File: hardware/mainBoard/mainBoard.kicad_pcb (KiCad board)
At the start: 2 copper layers, 99.9 x 49.9 mm, 22 parts, among them J1 DisplayConnector, J2 LeftKeyConnector, J3 RightKeyConnector, J4 EncoderConnector

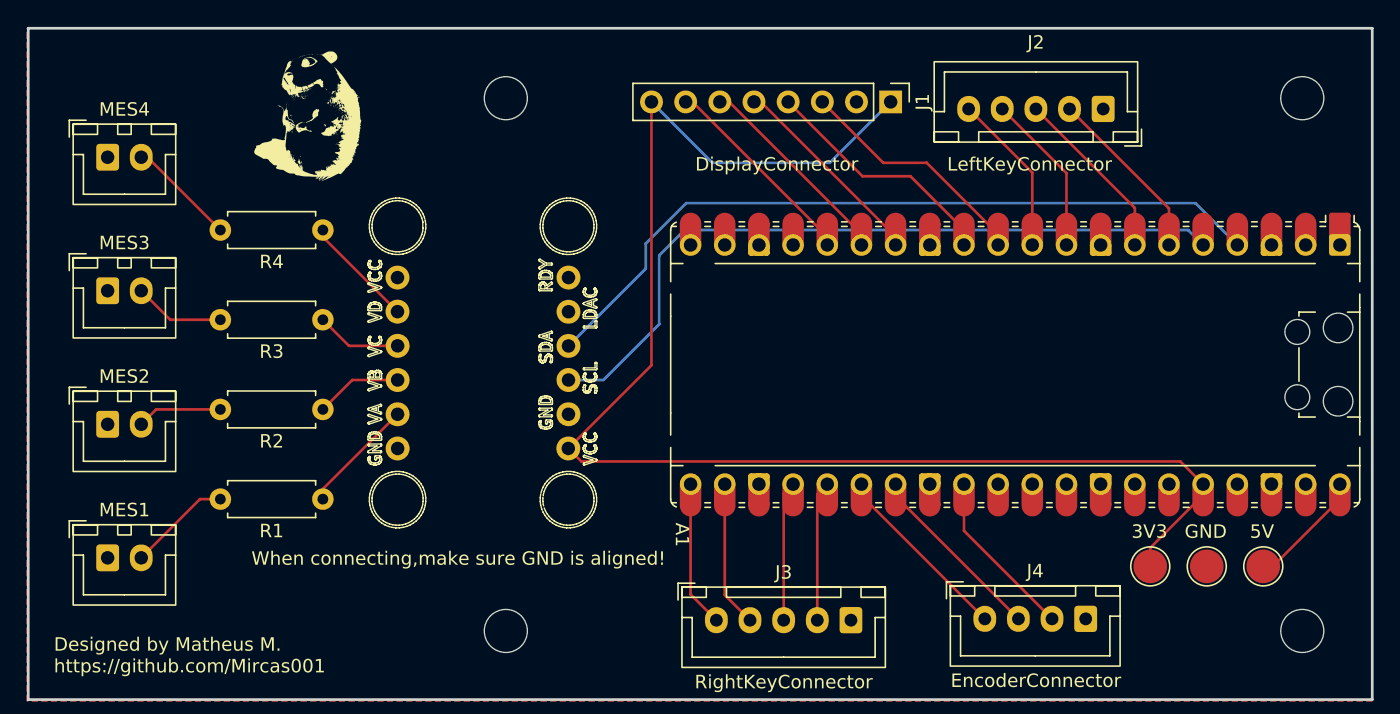
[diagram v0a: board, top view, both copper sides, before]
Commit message: Switched from prebuilt module to chip
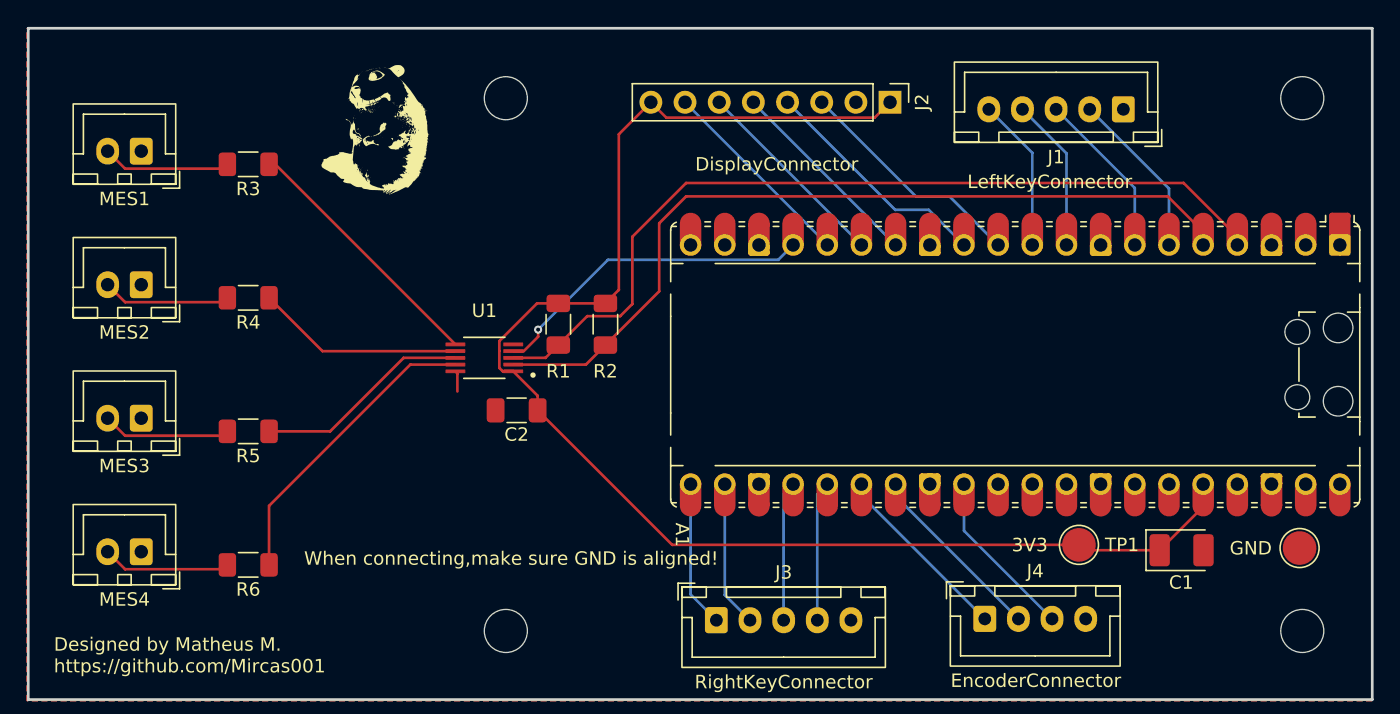
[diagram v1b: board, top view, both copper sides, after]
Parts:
- removed TP3: TestPoint, TestPoint:TestPoint_Pad_D2.5mm
- added C1: 10µF, Capacitor_Tantalum_SMD:CP_EIA-3528-15_AVX-H_HandSolder, F.Cu at (193.8, 108.8)
- added C2: 0.1μF, Capacitor_SMD:C_1206_3216Metric_Pad1.33x1.80mm_HandSolder, F.Cu at (144.4, 98.4)
- added R5: 680, Resistor_SMD:R_1206_3216Metric_Pad1.30x1.75mm_HandSolder, F.Cu at (124.5, 100.0)
- added R6: 680, Resistor_SMD:R_1206_3216Metric_Pad1.30x1.75mm_HandSolder, F.Cu at (124.5, 109.9)
- J1: value DisplayConnector -> LeftKeyConnector; footprint Connector_PinHeader_2.54mm:PinHeader_1x08_P2.54mm_Vertical -> Connector_JST:JST_XH_B5B-XH-A_1x05_P2.50mm_Vertical
- J2: value LeftKeyConnector -> DisplayConnector; footprint Connector_JST:JST_XH_B5B-XH-A_1x05_P2.50mm_Vertical -> Connector_PinHeader_2.54mm:PinHeader_1x08_P2.54mm_Vertical
- R1, R2: value 680 -> 10K; footprint Resistor_THT:R_Axial_DIN0207_L6.3mm_D2.5mm_P7.62mm_Horizontal -> Resistor_SMD:R_1206_3216Metric_Pad1.30x1.75mm_HandSolder
- R3, R4: footprint Resistor_THT:R_Axial_DIN0207_L6.3mm_D2.5mm_P7.62mm_Horizontal -> Resistor_SMD:R_1206_3216Metric_Pad1.30x1.75mm_HandSolder
- U1: value ~ -> MCP4728-E_UN; footprint Adafruit_MCP4728:Adafruit_MCP4728 -> Snapeda:SOP50P490X110-10N
- moved MES1 30.3 mm to (116.5, 79.1), turned to 180 degrees
- moved MES4 29.4 mm to (116.5, 108.9), turned to 180 degrees
- moved R2 21.9 mm to (151.0, 92.0), turned to -90 degrees
- moved R1 21.8 mm to (147.5, 92.0), turned to -90 degrees
- moved J1 17.3 mm to (189.5, 76.0), turned to 180 degrees
- moved J2 15.8 mm to (172.2, 75.5), turned to -90 degrees
- moved U1 15.8 mm to (142.0, 94.5), turned to 180 degrees
- moved TP1 13.8 mm to (186.2, 108.4), turned to 0 degrees
- moved R3 12.8 mm to (124.5, 80.1)
- moved MES2 10.7 mm to (116.5, 89.1), turned to 180 degrees
- moved MES3 9.80 mm to (116.5, 99.0), turned to 180 degrees
- moved R4 7.50 mm to (124.5, 90.0)
- moved TP2 7.03 mm to (202.6, 108.6)
- moved G*** 5.10 mm to (134.0, 78.0)
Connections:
- A1 pad 17: unconnected-(A1-GPIO13-Pad17) -> /LDAC
- J1 pad 1: +3V3 -> GND
- J1 pad 2: GND -> Net-(A1-GPIO4)
- J1 pad 3: Net-(A1-GPIO8) -> Net-(A1-GPIO5)
- J1 pad 4: Net-(A1-GPIO9) -> Net-(A1-GPIO6)
- J1 pad 5: Net-(A1-GPIO10) -> Net-(A1-GPIO7)
- J2 pad 1: GND -> +3V3
- J2 pad 2: Net-(A1-GPIO4) -> GND
- J2 pad 3: Net-(A1-GPIO5) -> Net-(A1-GPIO8)
- J2 pad 4: Net-(A1-GPIO6) -> Net-(A1-GPIO9)
- J2 pad 5: Net-(A1-GPIO7) -> Net-(A1-GPIO10)
- R1 pad 1: Net-(U1-VA) -> +3V3
- R1 pad 2: Net-(MES1-+) -> SDA
- R2 pad 1: Net-(U1-VB) -> +3V3
- R2 pad 2: Net-(MES2-+) -> SCL
- R3 pad 1: Net-(U1-VC) -> Net-(U1-VOUTA)
- R3 pad 2: Net-(MES3-+) -> Net-(MES1-+)
- R4 pad 1: Net-(U1-VD) -> Net-(U1-VOUTB)
- R4 pad 2: Net-(MES4-+) -> Net-(MES2-+)
- TP1 pad 1: +5V -> +3V3
- U1 pad 1: GND -> +3V3
- U1 pad 10: SDA -> GND
- U1 pad 2: Net-(U1-VA) -> SCL
- U1 pad 3: Net-(U1-VB) -> SDA
- U1 pad 4: Net-(U1-VC) -> /LDAC
- U1 pad 5: Net-(U1-VD) -> unconnected-(U1-RDY/*BSY-Pad5)
- U1 pad 6: unconnected-(U1-VCC-Pad6) -> Net-(U1-VOUTA)
- U1 pad 7: +3V3 -> Net-(U1-VOUTB)
- U1 pad 8: GND -> Net-(U1-VOUTC)
- U1 pad 9: SCL -> Net-(U1-VOUTD)
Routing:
- net /LDAC: track 0.00 -> 24.4 mm, vias 0 -> 1
- net Net-(U1-VOUTD): track 0.00 -> 22.6 mm
- net Net-(U1-VOUTA): track 0.00 -> 19.4 mm
- net Net-(U1-VOUTC): track 0.00 -> 16.1 mm
- net Net-(U1-VOUTB): track 0.00 -> 15.5 mm
- net +5V: track 9.61 -> 0.73 mm
- net Net-(U1-VA): track 8.61 -> 0.00 mm
- net Net-(U1-VD): track 8.36 -> 0.00 mm
- net SDA: track 56.5 -> 64.4 mm
- net Net-(U1-VB): track 6.46 -> 0.00 mm
- net Net-(U1-VC): track 6.36 -> 0.00 mm
- net SCL: track 55.2 -> 61.5 mm
- net Net-(MES2-+): track 6.34 -> 9.57 mm
- net Net-(MES3-+): track 6.77 -> 9.57 mm
- net +3V3: track 105.5 -> 107.7 mm
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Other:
- board text removed: "5V"

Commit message: update README.md to have kicanvas and 3d model image, also fix main board PCB
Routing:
- net +3V3: track 107.7 -> 123.9 mm, vias 0 -> 1
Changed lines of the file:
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@@
 	)
 	(footprint "Snapeda:SOP50P490X110-10N"
-		(locked yes)
 		(layer "F.Cu")
 		(at 142 94.5 180)
@@
 			)
 		)
-		(pad "1" thru_hole rect
+		(pad "1" thru_hole oval
 			(at 0 0 270)
 			(size 1.7 1.7)
@@
 			(pintype "passive")
 		)
-		(pad "2" thru_hole circle
-			(at 0 2.54 270)
+		(pad "2" thru_hole roundrect
+			(at 0 2.54)
 			(size 1.7 1.7)
 			(drill 1)
 			(layers "*.Cu" "*.Mask")
 			(remove_unused_layers no)
+			(roundrect_rratio 0.1470588235)
 			(net "GND")
 			(pinfunction "Pin_2_2")
@@
 	)
 	(segment
-		(start 154.38 75.5)
-		(end 155.53 76.65)
+		(start 159.48 80.6)
+		(end 154.38 75.5)
 		(width 0.2)
 		(layer "F.Cu")
@@
 	)
 	(segment
-		(start 155.53 76.65)
-		(end 171.01 76.65)
-		(width 0.2)
-		(layer "F.Cu")
-		(net "+3V3")
-	)
-	(segment
 		(start 143.115 94)
 		(end 143.115 95.244732)
@@
 	)
 	(segment
+		(start 178.6 80.6)
+		(end 159.48 80.6)
+		(width 0.2)
+		(layer "F.Cu")
+		(net "+3V3")
+	)
+	(segment
 		(start 152 77.88)
 		(end 154.38 75.5)
@@
 	)
 	(segment
-		(start 171.01 76.65)
-		(end 172.16 75.5)
-		(width 0.2)
-		(layer "F.Cu")
-		(net "+3V3")
-	)
-	(segment
 		(start 192.2 108.8)
 		(end 195.4325 105.5675)
@@
 		(net "+3V3")
 	)
+	(via
+		(at 178.6 80.6)
+		(size 0.6)
+		(drill 0.3)
+		(layers "F.Cu" "B.Cu")
+		(net "+3V3")
+	)
+	(segment
+		(start 175.2 77.2)
+		(end 173.86 77.2)
+		(width 0.2)
+		(layer "B.Cu")
+		(net "+3V3")
+	)
+	(segment
+		(start 173.86 77.2)
+		(end 172.16 75.5)
+		(width 0.2)
+		(layer "B.Cu")
+		(net "+3V3")
+	)
+	(segment
+		(start 178.6 80.6)
+		(end 175.2 77.2)
+		(width 0.2)
+		(layer "B.Cu")
+		(net "+3V3")
+	)

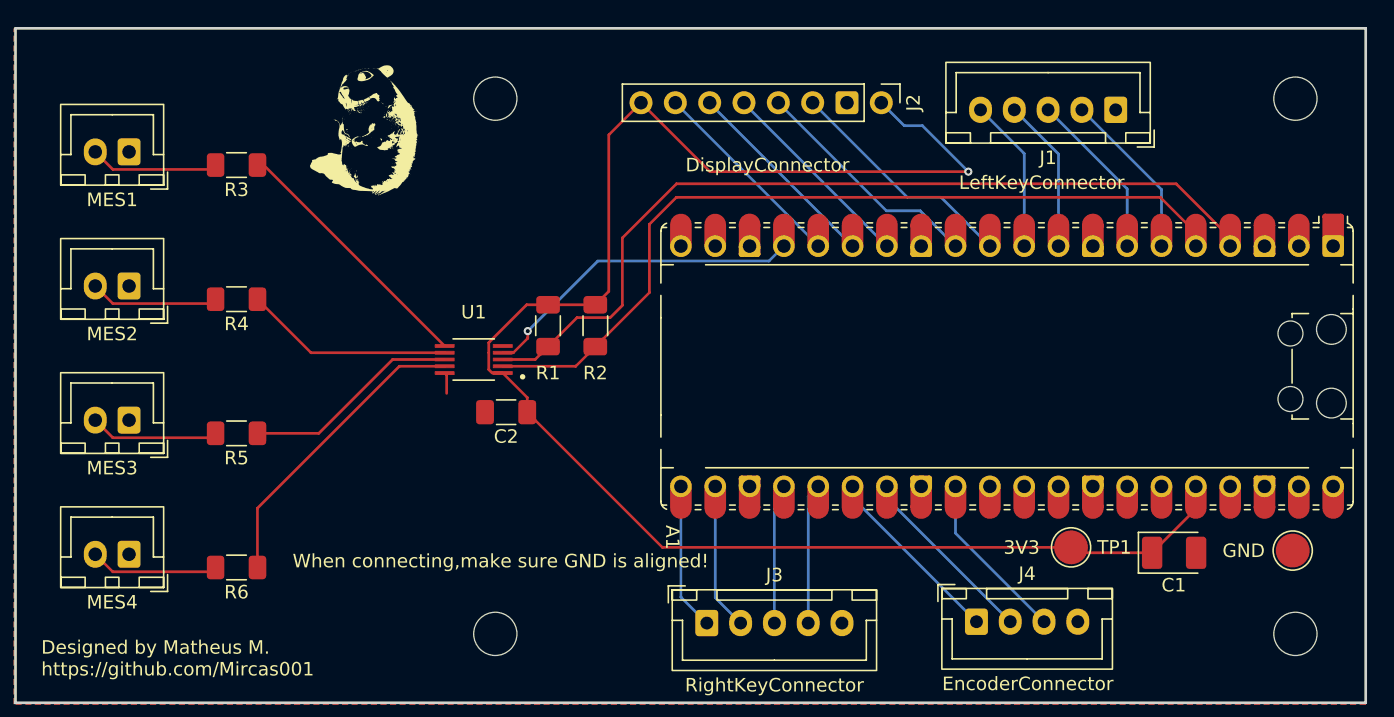
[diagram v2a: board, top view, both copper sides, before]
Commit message: Label the connectors in the silkscreen
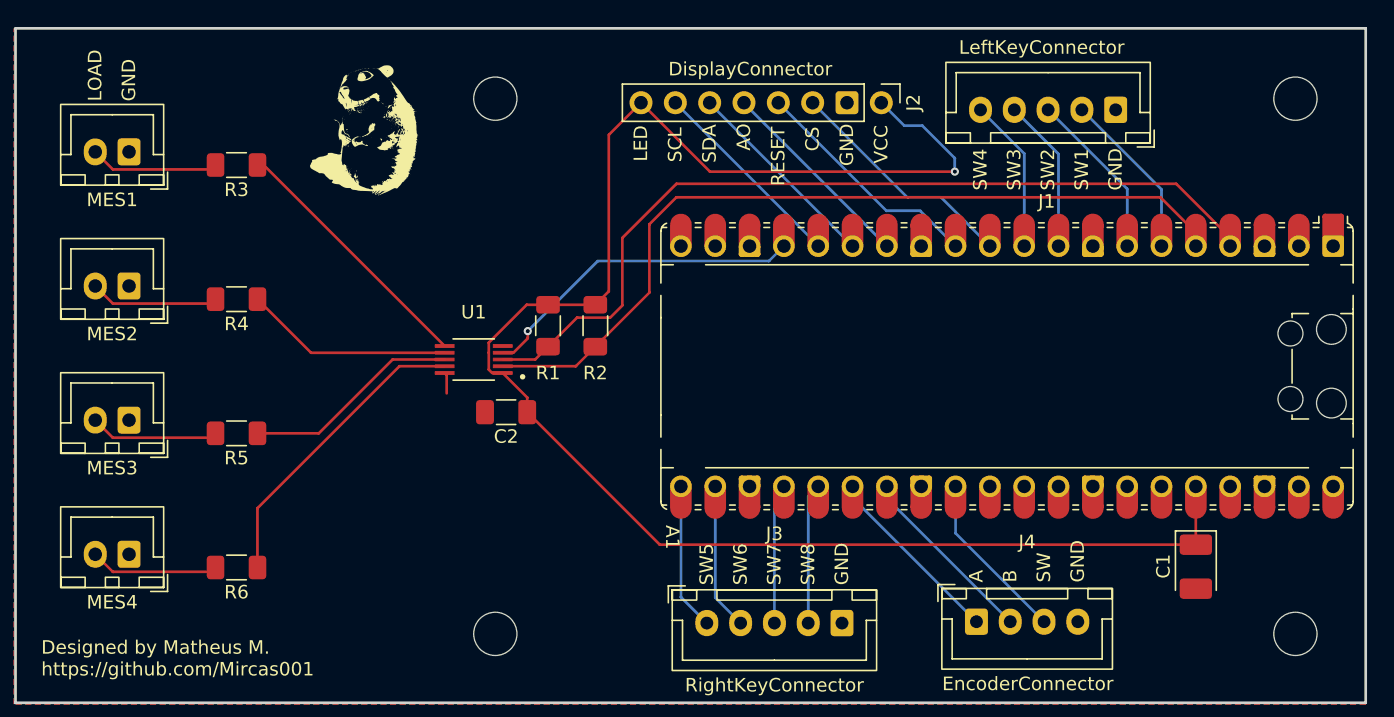
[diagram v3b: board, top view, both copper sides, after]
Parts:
- removed TP1, TP2: TestPoint, TestPoint:TestPoint_Pad_D2.5mm
- moved C1 1.91 mm to (195.4, 109.8), turned to -90 degrees
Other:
- board text added: "A"
- board text added: "AO"
- board text added: "B"
- board text added: "CS"
- board text added: "LED"
- board text added: "LOAD"
- board text added: "RESET"
- board text added: "SCL"
- board text added: "SDA"
- board text added: "SW"
- board text added: "SW1"
- board text added: "SW2"
- board text added: "SW3"
- board text added: "SW4"
- board text added: "SW5"
- board text added: "SW6"
- board text added: "SW7"
- board text added: "SW8"
- board text added: "VCC"
- board text removed: "3V3"
- board text removed: "When connecting,make sure GND is aligned!"

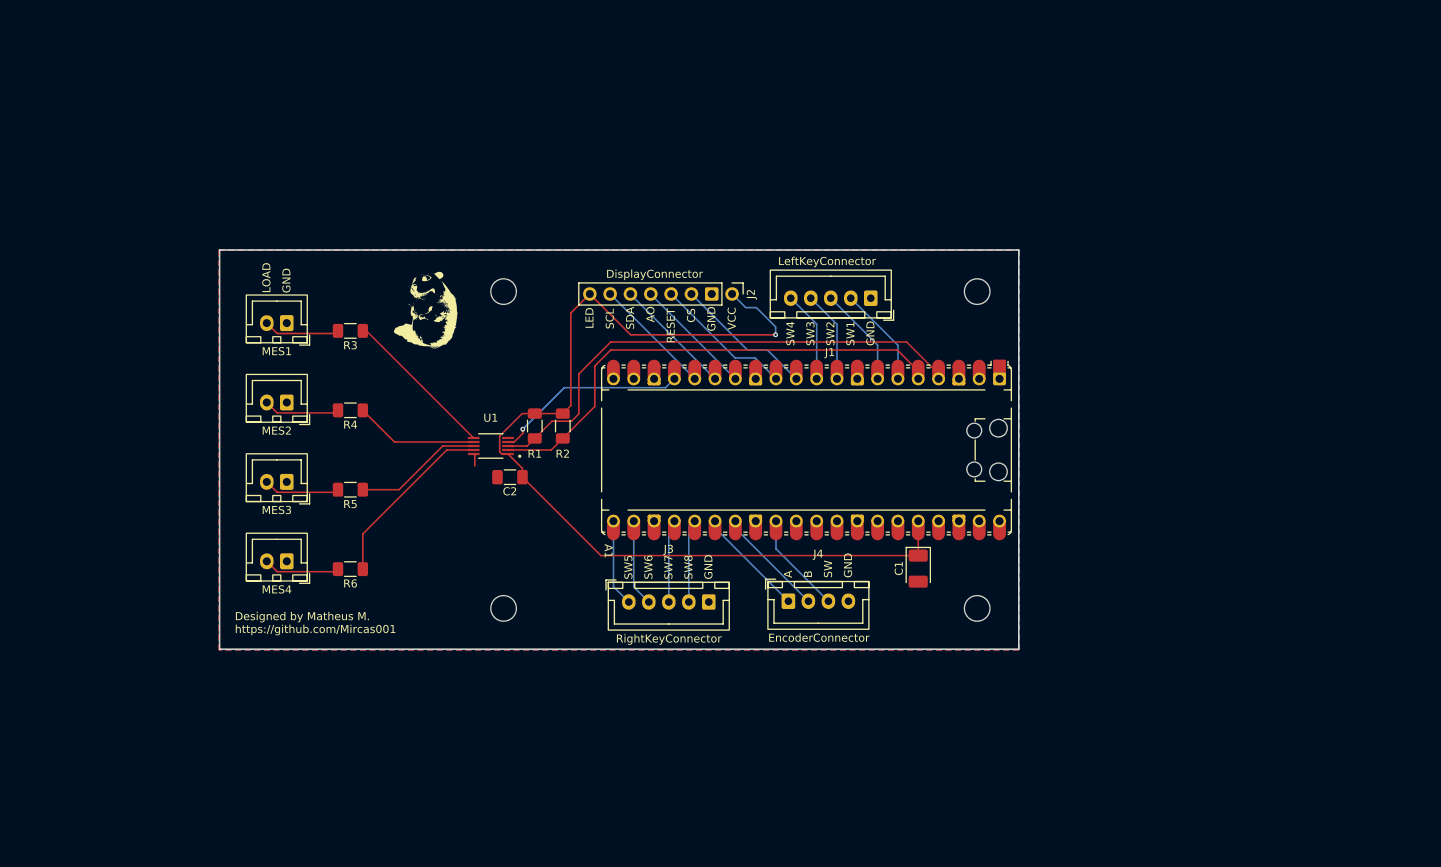
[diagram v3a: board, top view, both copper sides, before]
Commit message: update PCB routing and add debug probe
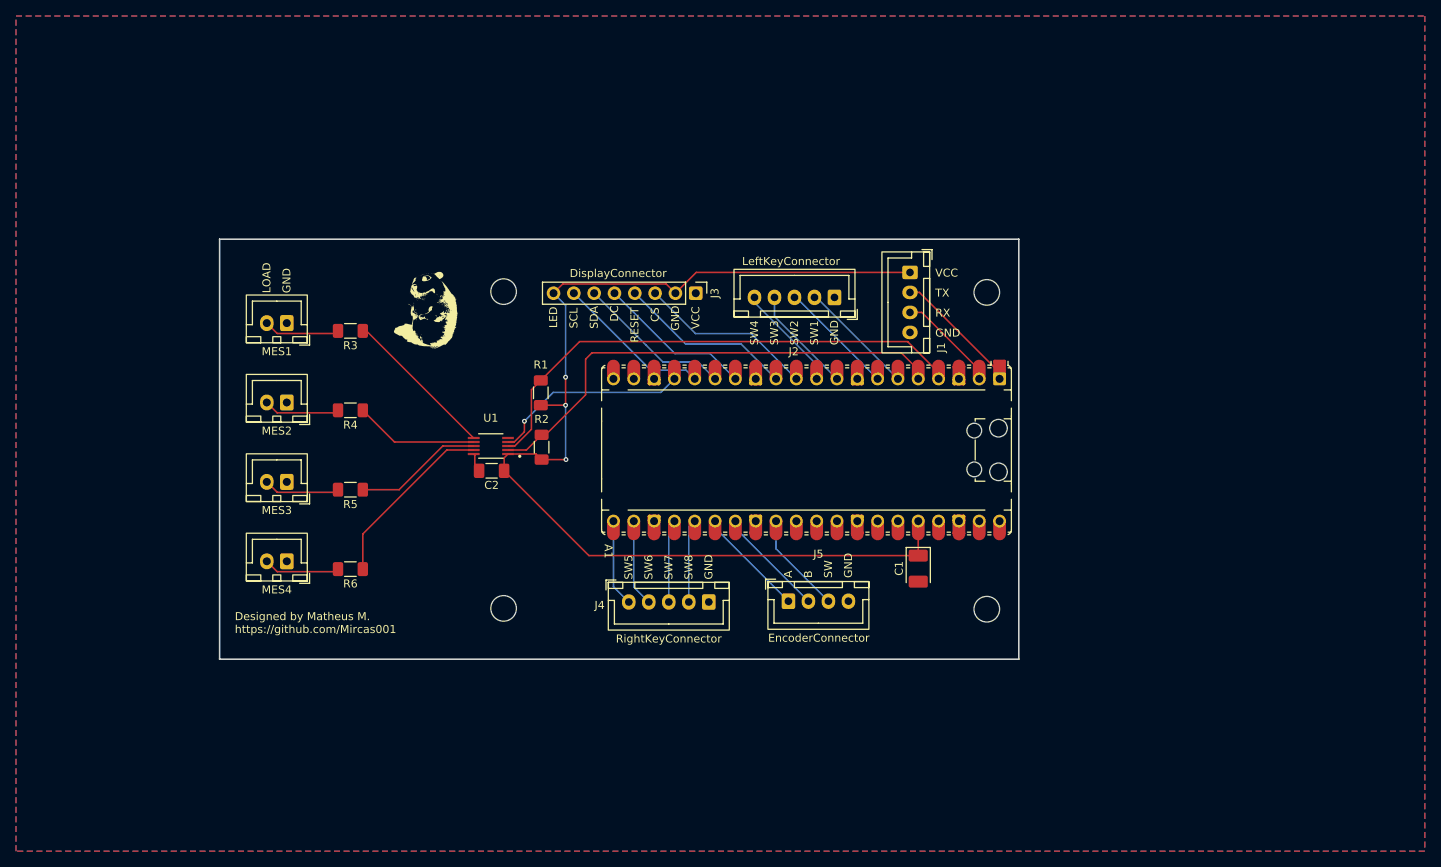
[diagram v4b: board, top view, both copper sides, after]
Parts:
- added J1: UARTDebug, Connector_JST:JST_XH_B4B-XH-A_1x04_P2.50mm_Vertical, F.Cu at (194.4, 72.8)
- C2: value 0.1μF -> 100nF
- moved J2 4.54 mm to (185.0, 75.9)
- moved J3 4.54 mm to (167.6, 75.4)
- moved R1 4.22 mm to (148.2, 87.8), turned to 90 degrees
- moved R2 3.75 mm to (148.3, 94.7), turned to 90 degrees
- moved C2 2.44 mm to (142.1, 97.6)
- moved REF** 1.20 mm to (204.0, 114.9)
- moved REF** 1.20 mm to (204.0, 75.3)
- renumbered J1 to J2, J2 to J3, J3 to J4, J4 to J5
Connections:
- A1 pad 1: unconnected-(A1-GPIO0-Pad1)_1 -> Net-(A1-GPIO0)
- A1 pad 2: unconnected-(A1-GPIO1-Pad2) -> Net-(A1-GPIO1)
- J3 pad 1: +3V3 -> GND
- J3 pad 2: GND -> +3V3
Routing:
- net +3V3: track 123.5 -> 141.5 mm, vias 1 -> 3
- net Net-(A1-GPIO0): track 0.00 -> 15.3 mm
- net Net-(A1-GPIO1): track 0.00 -> 12.8 mm
- net Net-(A1-GPIO8): track 17.5 -> 22.1 mm
- net Net-(A1-GPIO9): track 17.5 -> 22.1 mm
- net Net-(A1-GPIO11): track 15.8 -> 20.3 mm
- net Net-(A1-GPIO10): track 15.0 -> 19.5 mm
- net Net-(A1-GPIO12): track 15.8 -> 20.3 mm
- net Net-(A1-GPIO4): track 12.5 -> 14.7 mm
- net Net-(A1-GPIO5): track 12.5 -> 14.6 mm
- net Net-(A1-GPIO7): track 11.4 -> 13.4 mm
- net Net-(A1-GPIO6): track 11.4 -> 13.4 mm
- net SDA: track 64.4 -> 63.7 mm
- net SCL: track 61.5 -> 60.9 mm
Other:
- board size 99.9 x 49.9 mm -> 99.9 x 52.5 mm
- board text added: "DC"
- board text added: "RX"
- board text added: "TX"
- board text removed: "AO"
